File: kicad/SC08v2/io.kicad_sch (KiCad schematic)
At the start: 18 parts

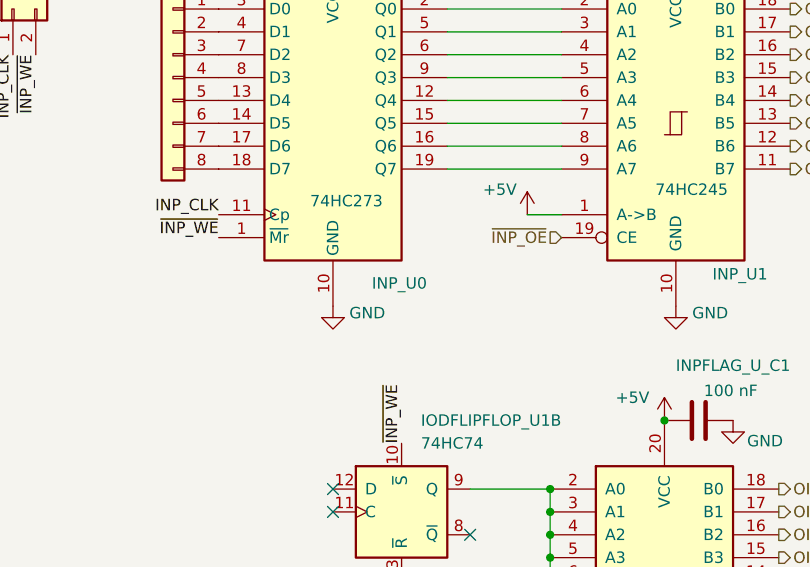
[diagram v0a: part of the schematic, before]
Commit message: Improve and fix docs
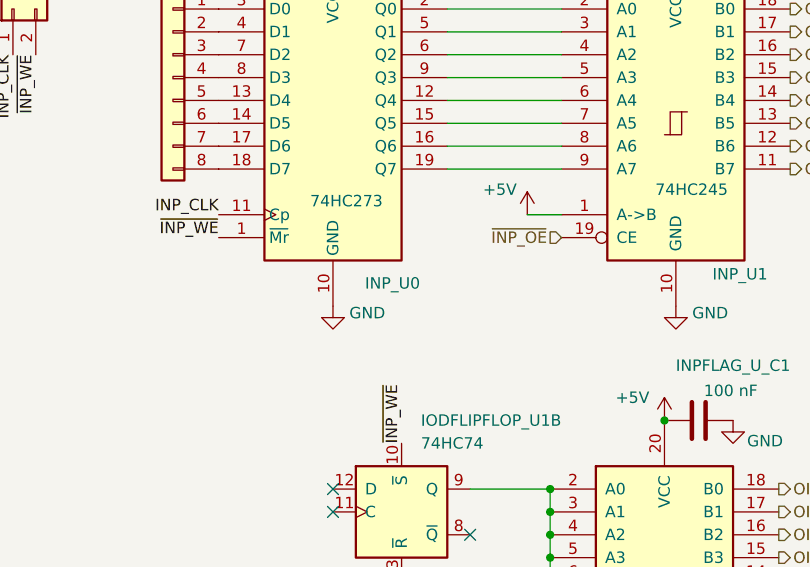
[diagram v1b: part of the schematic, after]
